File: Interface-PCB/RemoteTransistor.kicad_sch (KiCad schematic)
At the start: 23 parts, among them IC2 TBD62783APG, IC3 TBD62783APG, J13 CONN_05JST, J14 CONN_05JST, U3 CD74HC4067_MUX_BREAKOUT

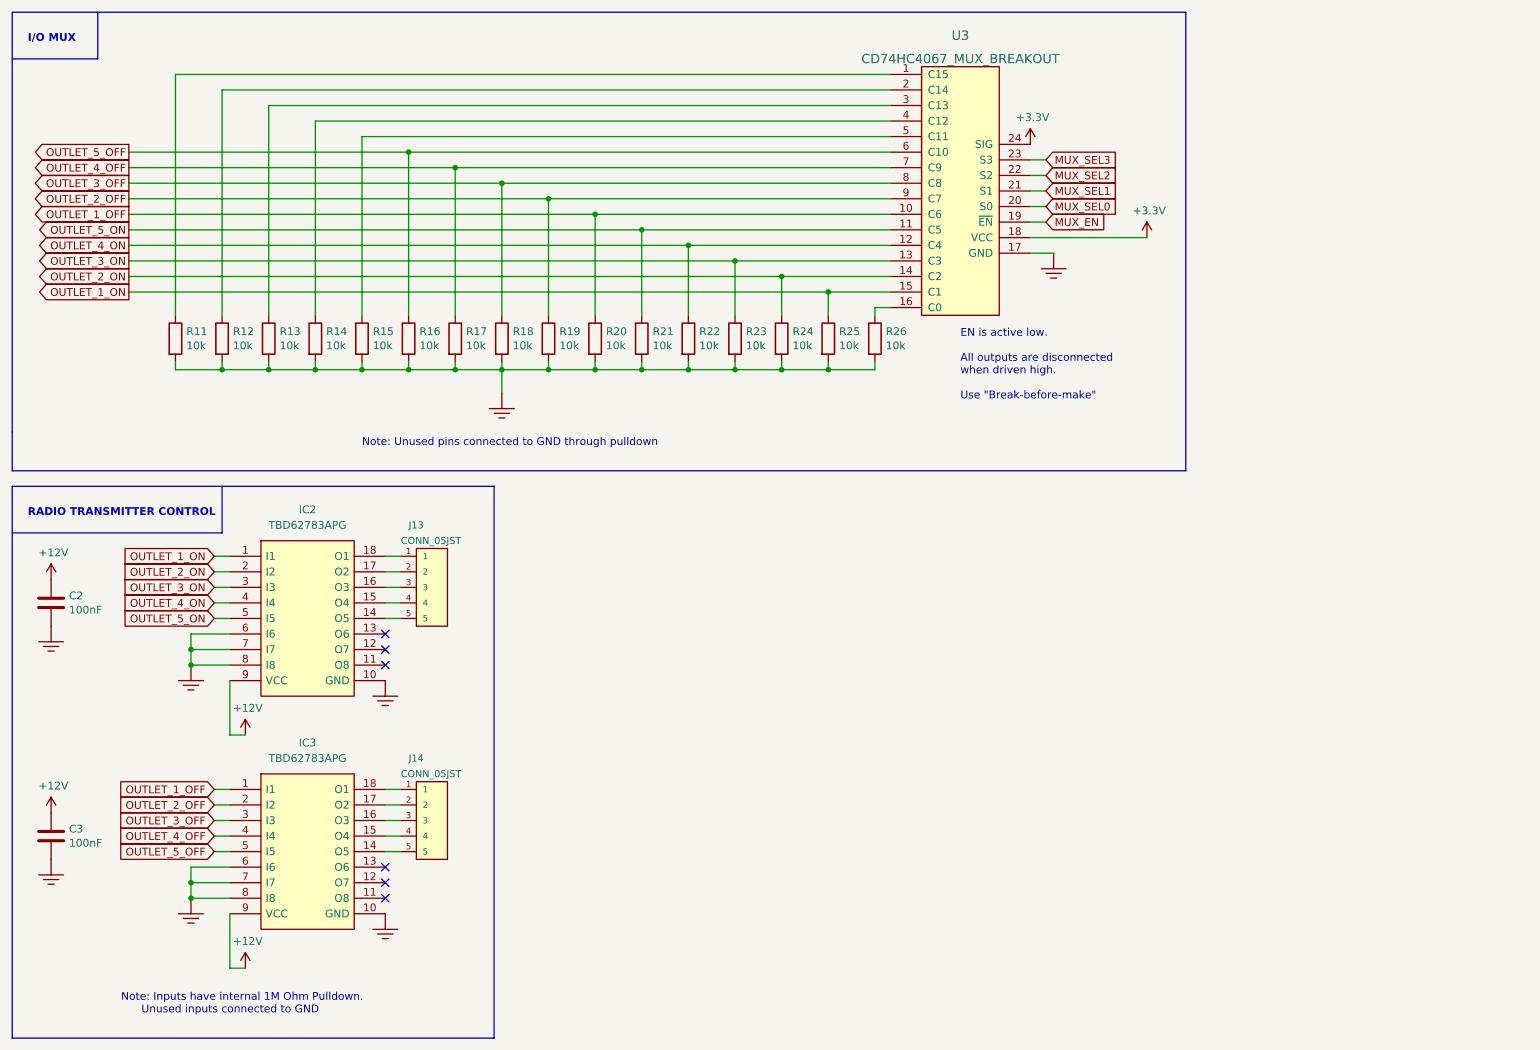
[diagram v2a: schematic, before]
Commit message: Start Rev 1.1, Add pulldowns on Mux Input
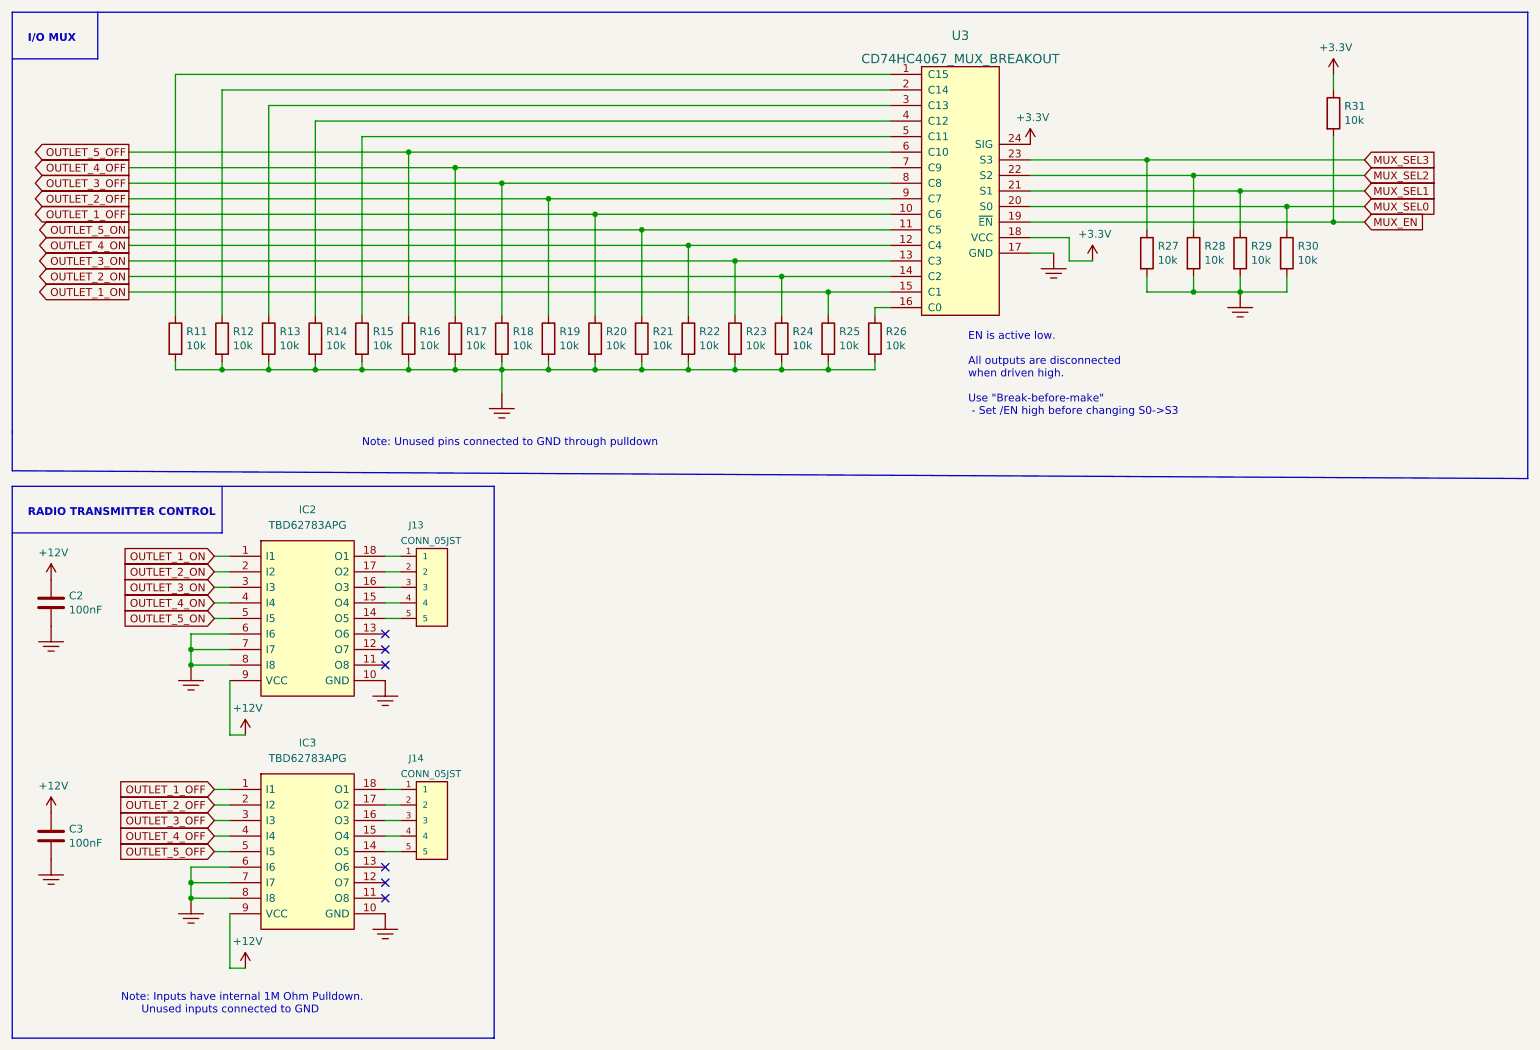
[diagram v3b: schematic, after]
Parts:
- added R27, R28, R29, R30, R31: 10k, AA_Custom_Components:R_SS_Axial_DIN0207_L6.3mm_D2.5mm_P10.16mm_Horizontal, symbol Device:R
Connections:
- net +3V3: now also R31.1
- net GND: now also R27.2, R28.2, R29.2, R30.2
- net MUX_EN: now also R31.2
- net MUX_SEL0: now also R30.1
- net MUX_SEL1: now also R29.1
- net MUX_SEL2: now also R28.1
- net MUX_SEL3: now also R27.1
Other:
- note added: "EN is active low. All outputs are disconnected when driven high. Use "Break-before-make" - Set /EN high before changing S0->S3"
- note removed: "EN is active low. All outputs are disconnected when driven high. Use "Break-before-make""
